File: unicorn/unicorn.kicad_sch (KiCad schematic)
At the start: 25 parts, among them J0 Conn_01x02, J1 Conn_01x14_Female, J2 Conn_01x14_Female, J3 Conn_02x03_Odd_Even, U1 ATmega328-P, U2 L7805

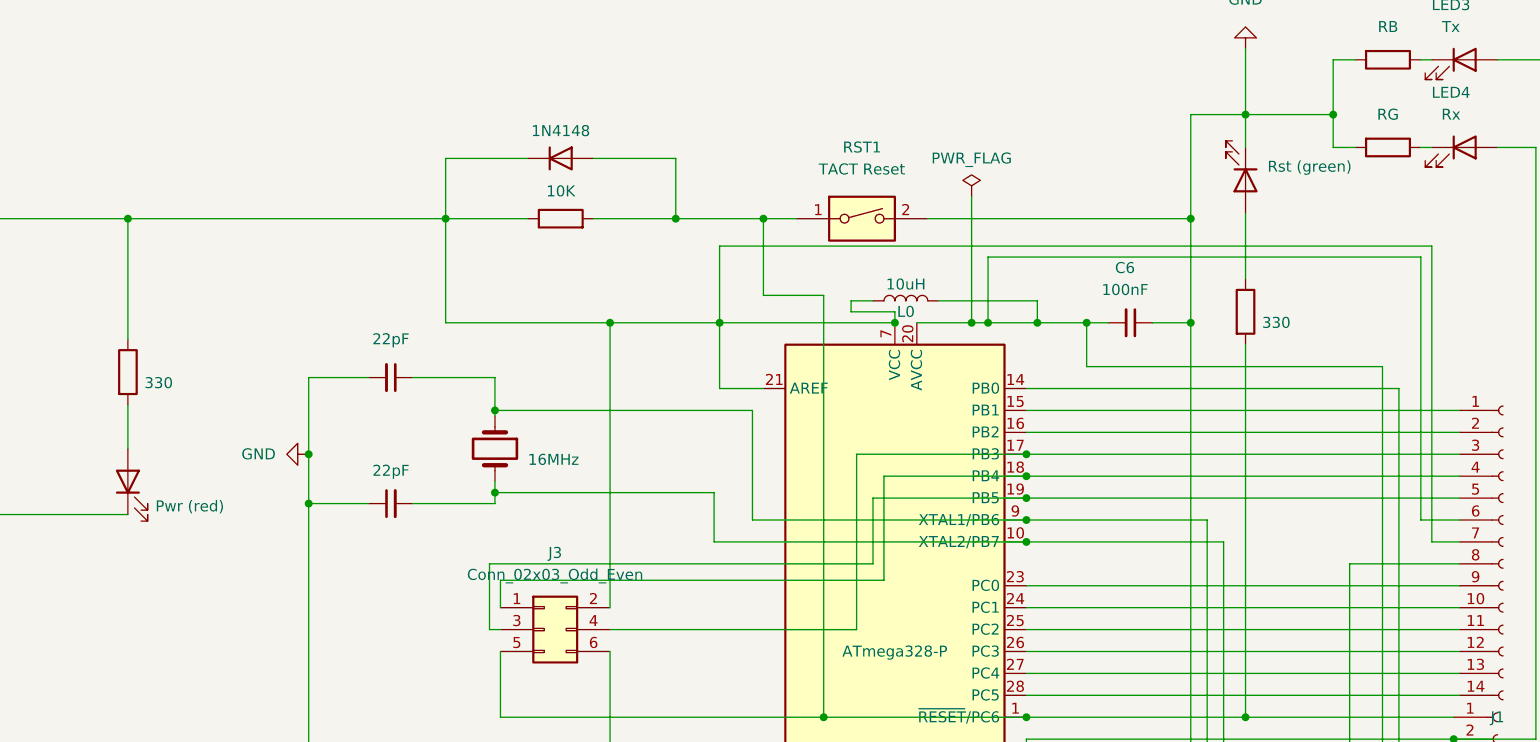
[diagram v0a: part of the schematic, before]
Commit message: add fp anch sym table settings and fix the projects
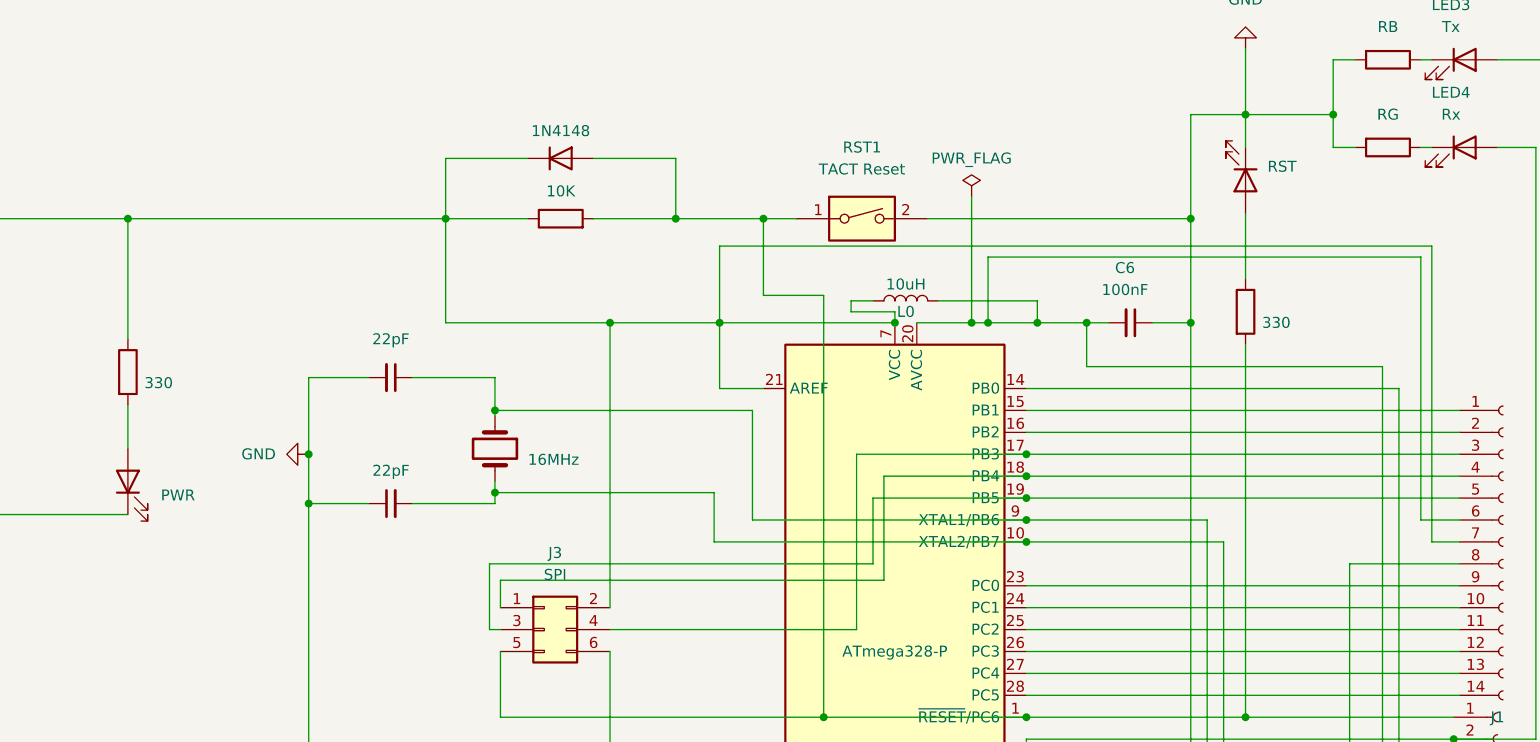
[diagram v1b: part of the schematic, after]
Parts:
- J3: value Conn_02x03_Odd_Even -> SPI
- LED1: value Pwr (red) -> PWR
- LED2: value Rst (green) -> RST
- U2: footprint Transistor_Power_Module:TO255P1020X450X2000-3 -> L7805:TO255P1020X450X2000-3
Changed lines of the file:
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@@
   )
   (symbol (lib_id "Connector_Generic:Conn_02x03_Odd_Even") (at 158.75 102.87 0) (unit 1)
-    (in_bom yes) (on_board yes) (dnp no) (fields_autoplaced)
+    (in_bom yes) (on_board yes) (dnp no)
     (property "Reference" "J3" (at 160.02 93.98 0)
       (effects (font (size 1.27 1.27)))
     )
-    (property "Value" "Conn_02x03_Odd_Even" (at 160.02 96.52 0)
+    (property "Value" "SPI" (at 160.02 96.52 0)
       (effects (font (size 1.27 1.27)))
     )
@@
       (effects (font (size 1.27 1.27)) (justify left) hide)
     )
-    (property "Value" "Rst (green)" (at 242.57 49.2124 90)
+    (property "Value" "RST" (at 242.57 49.2125 90)
       (effects (font (size 1.27 1.27)) (justify left))
     )
@@
       (effects (font (size 1.27 1.27)))
     )
-    (property "Footprint" "Transistor_Power_Module:TO255P1020X450X2000-3" (at 55.245 59.055 0)
+    (property "Footprint" "L7805:TO255P1020X450X2000-3" (at 55.245 59.055 0)
       (effects (font (size 1.27 1.27) italic) (justify left) hide)
     )
@@
       (effects (font (size 1.27 1.27)) (justify right) hide)
     )
-    (property "Value" "Pwr (red)" (at 113.665 88.5824 90)
+    (property "Value" "PWR" (at 114.3 87.3125 90)
       (effects (font (size 1.27 1.27)) (justify right))
     )

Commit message: replace power connector - still need to redo routing
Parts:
- J0: footprint Connector_JST:JST_PH_S2B-PH-K_1x02_P2.00mm_Horizontal -> Connector_JST:JST_PH_S2B-PH-SM4-TB_1x02-1MP_P2.00mm_Horizontal
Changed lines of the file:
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@@
       (effects (font (size 1.27 1.27)) (justify left))
     )
-    (property "Footprint" "Connector_JST:JST_PH_S2B-PH-K_1x02_P2.00mm_Horizontal" (at 33.655 31.75 0)
+    (property "Footprint" "Connector_JST:JST_PH_S2B-PH-SM4-TB_1x02-1MP_P2.00mm_Horizontal" (at 33.655 31.75 0)
       (effects (font (size 1.27 1.27)) hide)
     )

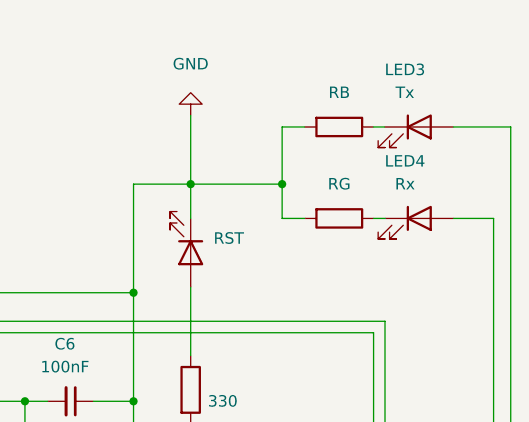
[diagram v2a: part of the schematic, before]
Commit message: fix routing + replace power connector with the right one
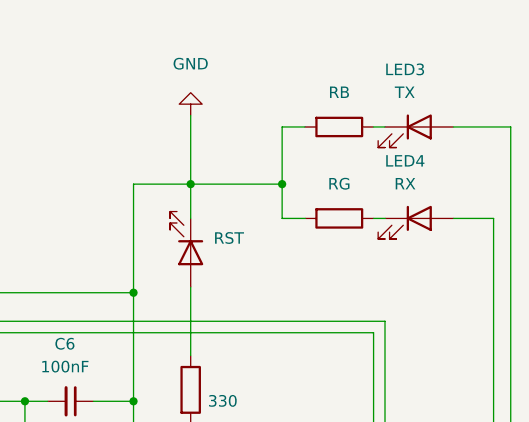
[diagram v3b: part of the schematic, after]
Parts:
- J0: footprint Connector_JST:JST_PH_S2B-PH-SM4-TB_1x02-1MP_P2.00mm_Horizontal -> JST_S2B-PH-SM4-TB:JST_S2B-PH-SM4-TB
- LED3: value Tx -> TX
- LED4: value Rx -> RX
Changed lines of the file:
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@@
     (title "Unicorn")
     (date "2023-08-03")
-    (rev "A")
+    (rev "B")
     (comment 1 "Author: Simone Girardi")
   )
@@
       (effects (font (size 1.27 1.27)))
     )
-    (property "Value" "Rx" (at 263.8425 43.18 0)
+    (property "Value" "RX" (at 263.8425 43.18 0)
       (effects (font (size 1.27 1.27)))
     )
@@
       (effects (font (size 1.27 1.27)) (justify left))
     )
-    (property "Footprint" "Connector_JST:JST_PH_S2B-PH-SM4-TB_1x02-1MP_P2.00mm_Horizontal" (at 33.655 31.75 0)
+    (property "Footprint" "JST_S2B-PH-SM4-TB:JST_S2B-PH-SM4-TB" (at 33.655 31.75 0)
       (effects (font (size 1.27 1.27)) hide)
     )
@@
       (effects (font (size 1.27 1.27)))
     )
-    (property "Value" "Tx" (at 263.8425 33.02 0)
-      (effects (font (size 1.27 1.27)))
-    )
+    (property "Value" "TX" (at 263.8425 33.02 0)
+      (effects (font (size 1.27 1.27)))
+    )

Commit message: update unicorn board layout - minor improvements to the project footprints
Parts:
- RST1: value TACT Reset -> Reset
- renumbered J0 to J1, J3 to J2, J2 to J3, J1 to J4, L0 to L1, U2 to U1, U1 to U2
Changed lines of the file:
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@@
   (symbol (lib_id "power:GND") (at 131.445 82.55 270) (unit 1)
     (in_bom yes) (on_board yes) (dnp no) (fields_autoplaced)
-    (property "Reference" "#PWR0101" (at 125.095 82.55 0)
+    (property "Reference" "#PWR02" (at 125.095 82.55 0)
       (effects (font (size 1.27 1.27)) hide)
     )
@@
       (project "unicorn"
         (path "/b0d906b8-ab9f-434d-bec4-be0d48b77c08"
-          (reference "#PWR0101") (unit 1)
+          (reference "#PWR02") (unit 1)
         )
       )
@@
   (symbol (lib_id "MCU_Microchip_ATmega:ATmega328-P") (at 199.39 105.41 0) (unit 1)
     (in_bom yes) (on_board yes) (dnp no)
-    (property "Reference" "U1" (at 178.435 70.5993 0)
+    (property "Reference" "U2" (at 178.435 70.5993 0)
       (effects (font (size 1.27 1.27)) hide)
     )
@@
       (project "unicorn"
         (path "/b0d906b8-ab9f-434d-bec4-be0d48b77c08"
-          (reference "U1") (unit 1)
+          (reference "U2") (unit 1)
         )
       )
@@
   (symbol (lib_id "power:GND") (at 240.03 35.56 180) (unit 1)
     (in_bom yes) (on_board yes) (dnp no) (fields_autoplaced)
-    (property "Reference" "#PWR0104" (at 240.03 29.21 0)
+    (property "Reference" "#PWR03" (at 240.03 29.21 0)
       (effects (font (size 1.27 1.27)) hide)
     )
@@
       (project "unicorn"
         (path "/b0d906b8-ab9f-434d-bec4-be0d48b77c08"
-          (reference "#PWR0104") (unit 1)
+          (reference "#PWR03") (unit 1)
         )
       )
@@
   (symbol (lib_id "power:PWR_FLAG") (at 208.28 52.705 0) (unit 1)
     (in_bom yes) (on_board yes) (dnp no) (fields_autoplaced)
-    (property "Reference" "#FLG01" (at 208.28 50.8 0)
+    (property "Reference" "#FLG03" (at 208.28 50.8 0)
       (effects (font (size 1.27 1.27)) hide)
     )
@@
       (project "unicorn"
         (path "/b0d906b8-ab9f-434d-bec4-be0d48b77c08"
-          (reference "#FLG01") (unit 1)
+          (reference "#FLG03") (unit 1)
         )
       )
@@
   (symbol (lib_id "Connector_Generic:Conn_02x03_Odd_Even") (at 158.75 102.87 0) (unit 1)
     (in_bom yes) (on_board yes) (dnp no)
-    (property "Reference" "J3" (at 160.02 93.98 0)
+    (property "Reference" "J2" (at 160.02 93.98 0)
       (effects (font (size 1.27 1.27)))
     )
@@
       (project "unicorn"
         (path "/b0d906b8-ab9f-434d-bec4-be0d48b77c08"
-          (reference "J3") (unit 1)
+          (reference "J2") (unit 1)
         )
       )
@@
   (symbol (lib_id "Regulator_Linear:L7805") (at 54.61 55.245 0) (unit 1)
     (in_bom yes) (on_board yes) (dnp no) (fields_autoplaced)
-    (property "Reference" "U2" (at 54.61 47.625 0)
+    (property "Reference" "U1" (at 54.61 47.625 0)
       (effects (font (size 1.27 1.27)))
     )
@@
       (project "unicorn"
         (path "/b0d906b8-ab9f-434d-bec4-be0d48b77c08"
-          (reference "U2") (unit 1)
+          (reference "U1") (unit 1)
         )
       )
@@
   (symbol (lib_id "Connector:Conn_01x14_Socket") (at 269.24 128.27 0) (unit 1)
     (in_bom yes) (on_board yes) (dnp no) (fields_autoplaced)
-    (property "Reference" "J2" (at 268.605 149.225 0)
+    (property "Reference" "J3" (at 268.605 149.225 0)
       (effects (font (size 1.27 1.27)))
     )
@@
       (project "unicorn"
         (path "/b0d906b8-ab9f-434d-bec4-be0d48b77c08"
-          (reference "J2") (unit 1)
+          (reference "J3") (unit 1)
         )
       )
@@
   (symbol (lib_id "power:GND") (at 54.61 104.14 0) (unit 1)
     (in_bom yes) (on_board yes) (dnp no) (fields_autoplaced)
-    (property "Reference" "#PWR0103" (at 54.61 110.49 0)
+    (property "Reference" "#PWR01" (at 54.61 110.49 0)
       (effects (font (size 1.27 1.27)) hide)
     )
@@
       (project "unicorn"
         (path "/b0d906b8-ab9f-434d-bec4-be0d48b77c08"
-          (reference "#PWR0103") (unit 1)
+          (reference "#PWR01") (unit 1)
         )
       )
@@
     (in_bom yes) (on_board yes) (dnp no)
     (property "Reference" "D1" (at 160.655 41.275 0)
-      (effects (font (size 1.27 1.27)) hide)
+      (effects (font (size 1.27 1.27)))
     )
     (property "Value" "1N4148" (at 160.655 45.085 0)
@@
       (effects (font (size 1.27 1.27)))
     )
-    (property "Value" "TACT Reset" (at 195.58 49.53 0)
+    (property "Value" "Reset" (at 195.58 49.53 0)
       (effects (font (size 1.27 1.27)))
     )
@@
   (symbol (lib_id "Connector_Generic:Conn_01x02") (at 33.655 31.75 270) (mirror x) (unit 1)
     (in_bom yes) (on_board yes) (dnp no)
-    (property "Reference" "J0" (at 26.035 26.035 90)
+    (property "Reference" "J1" (at 26.035 26.035 90)
       (effects (font (size 1.27 1.27)) (justify left))
     )
@@
       (project "unicorn"
         (path "/b0d906b8-ab9f-434d-bec4-be0d48b77c08"
-          (reference "J0") (unit 1)
+          (reference "J1") (unit 1)
         )
       )
@@
   (symbol (lib_id "power:PWR_FLAG") (at 41.275 46.99 0) (unit 1)
     (in_bom yes) (on_board yes) (dnp no) (fields_autoplaced)
-    (property "Reference" "#FLG0101" (at 41.275 45.085 0)
+    (property "Reference" "#FLG01" (at 41.275 45.085 0)
       (effects (font (size 1.27 1.27)) hide)
     )
@@
       (project "unicorn"
         (path "/b0d906b8-ab9f-434d-bec4-be0d48b77c08"
-          (reference "#FLG0101") (unit 1)
+          (reference "#FLG01") (unit 1)
         )
       )
@@
   (symbol (lib_id "power:PWR_FLAG") (at 199.39 151.765 180) (unit 1)
     (in_bom yes) (on_board yes) (dnp no) (fields_autoplaced)
-    (property "Reference" "#FLG0102" (at 199.39 153.67 0)
+    (property "Reference" "#FLG02" (at 199.39 153.67 0)
       (effects (font (size 1.27 1.27)) hide)
     )
@@
       (project "unicorn"
         (path "/b0d906b8-ab9f-434d-bec4-be0d48b77c08"
-          (reference "#FLG0102") (unit 1)
+          (reference "#FLG02") (unit 1)
         )
       )
@@
   (symbol (lib_id "Device:L") (at 200.66 64.77 90) (unit 1)
     (in_bom yes) (on_board yes) (dnp no)
-    (property "Reference" "L0" (at 200.66 66.04 90)
+    (property "Reference" "L1" (at 200.66 66.04 90)
       (effects (font (size 1.27 1.27)))
     )
@@
       (project "unicorn"
         (path "/b0d906b8-ab9f-434d-bec4-be0d48b77c08"
-          (reference "L0") (unit 1)
+          (reference "L1") (unit 1)
         )
       )
@@
   (symbol (lib_id "Connector:Conn_01x14_Socket") (at 269.875 92.71 0) (unit 1)
     (in_bom yes) (on_board yes) (dnp no) (fields_autoplaced)
-    (property "Reference" "J1" (at 269.24 113.03 0)
+    (property "Reference" "J4" (at 269.24 113.03 0)
       (effects (font (size 1.27 1.27)))
     )
@@
       (project "unicorn"
         (path "/b0d906b8-ab9f-434d-bec4-be0d48b77c08"
-          (reference "J1") (unit 1)
-        )
-      )
+          (reference "J4") (unit 1)
+        )
+      )
